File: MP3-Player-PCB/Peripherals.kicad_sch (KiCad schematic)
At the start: 27 parts, among them J301 Micro_SD_Card_Det1, Q301 AO3401A, Q302 2N7002H, SW301 1-1825910-4, SW302 1-1825910-4, SW303 1-1825910-4, SW304 1-1825910-4, U301 TPD4E1U06

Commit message: Much better initial layout
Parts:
- C301, C304, C305: footprint Capacitor_SMD:C_0805_2012Metric -> Capacitor_SMD:C_0603_1608Metric
- C302, C303: footprint Capacitor_SMD:C_0603_1608Metric -> Capacitor_SMD:C_0402_1005Metric
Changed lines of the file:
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@@
 			)
 		)
-		(property "Footprint" "Capacitor_SMD:C_0603_1608Metric"
+		(property "Footprint" "Capacitor_SMD:C_0402_1005Metric"
 			(at 42.2148 58.42 0)
 			(effects
@@
 			)
 		)
-		(property "Footprint" "Capacitor_SMD:C_0603_1608Metric"
+		(property "Footprint" "Capacitor_SMD:C_0402_1005Metric"
 			(at 71.4248 83.82 0)
 			(effects
@@
 			)
 		)
-		(property "Footprint" "Capacitor_SMD:C_0805_2012Metric"
+		(property "Footprint" "Capacitor_SMD:C_0603_1608Metric"
 			(at 29.5148 58.42 0)
 			(effects
@@
 			)
 		)
-		(property "Footprint" "Capacitor_SMD:C_0805_2012Metric"
+		(property "Footprint" "Capacitor_SMD:C_0603_1608Metric"
 			(at 99.3648 137.16 0)
 			(effects
@@
 			)
 		)
-		(property "Footprint" "Capacitor_SMD:C_0805_2012Metric"
+		(property "Footprint" "Capacitor_SMD:C_0603_1608Metric"
 			(at 136.1948 138.43 0)
 			(effects

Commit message: Cleaned up layout yet again for proper routing. Started preliminary routing
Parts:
- R305, R306, R307: footprint Resistor_SMD:R_0603_1608Metric -> Resistor_SMD:R_0402_1005Metric
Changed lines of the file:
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@@
 			)
 		)
-		(property "Footprint" "Resistor_SMD:R_0603_1608Metric"
+		(property "Footprint" "Resistor_SMD:R_0402_1005Metric"
 			(at 91.44 47.498 90)
 			(effects
@@
 			)
 		)
-		(property "Footprint" "Resistor_SMD:R_0603_1608Metric"
+		(property "Footprint" "Resistor_SMD:R_0402_1005Metric"
 			(at 91.44 57.658 90)
 			(effects
@@
 			)
 		)
-		(property "Footprint" "Resistor_SMD:R_0603_1608Metric"
+		(property "Footprint" "Resistor_SMD:R_0402_1005Metric"
 			(at 91.44 52.578 90)
 			(effects

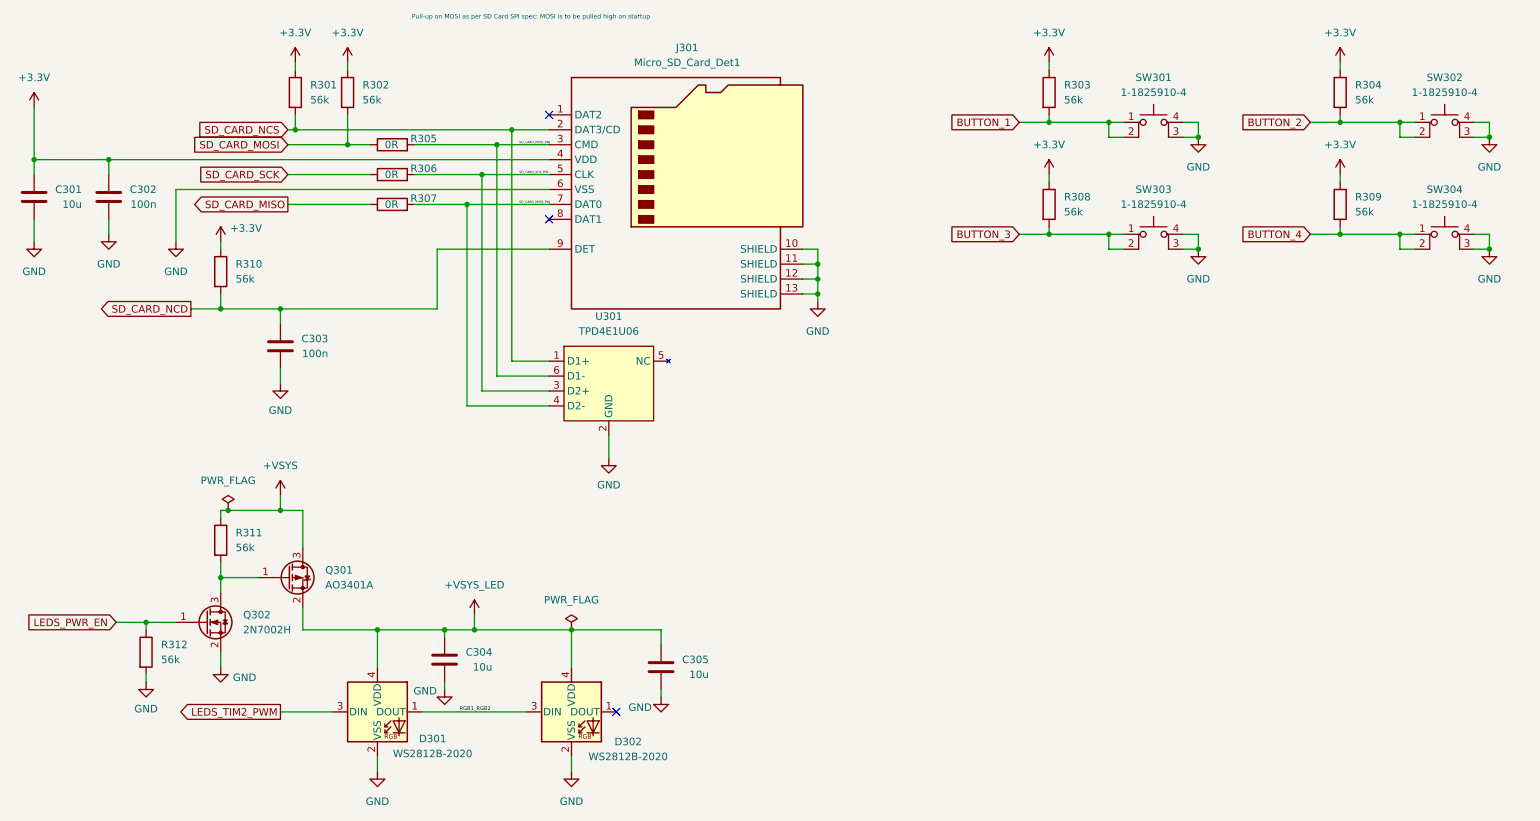
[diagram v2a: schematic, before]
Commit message: Routing more mcu signals
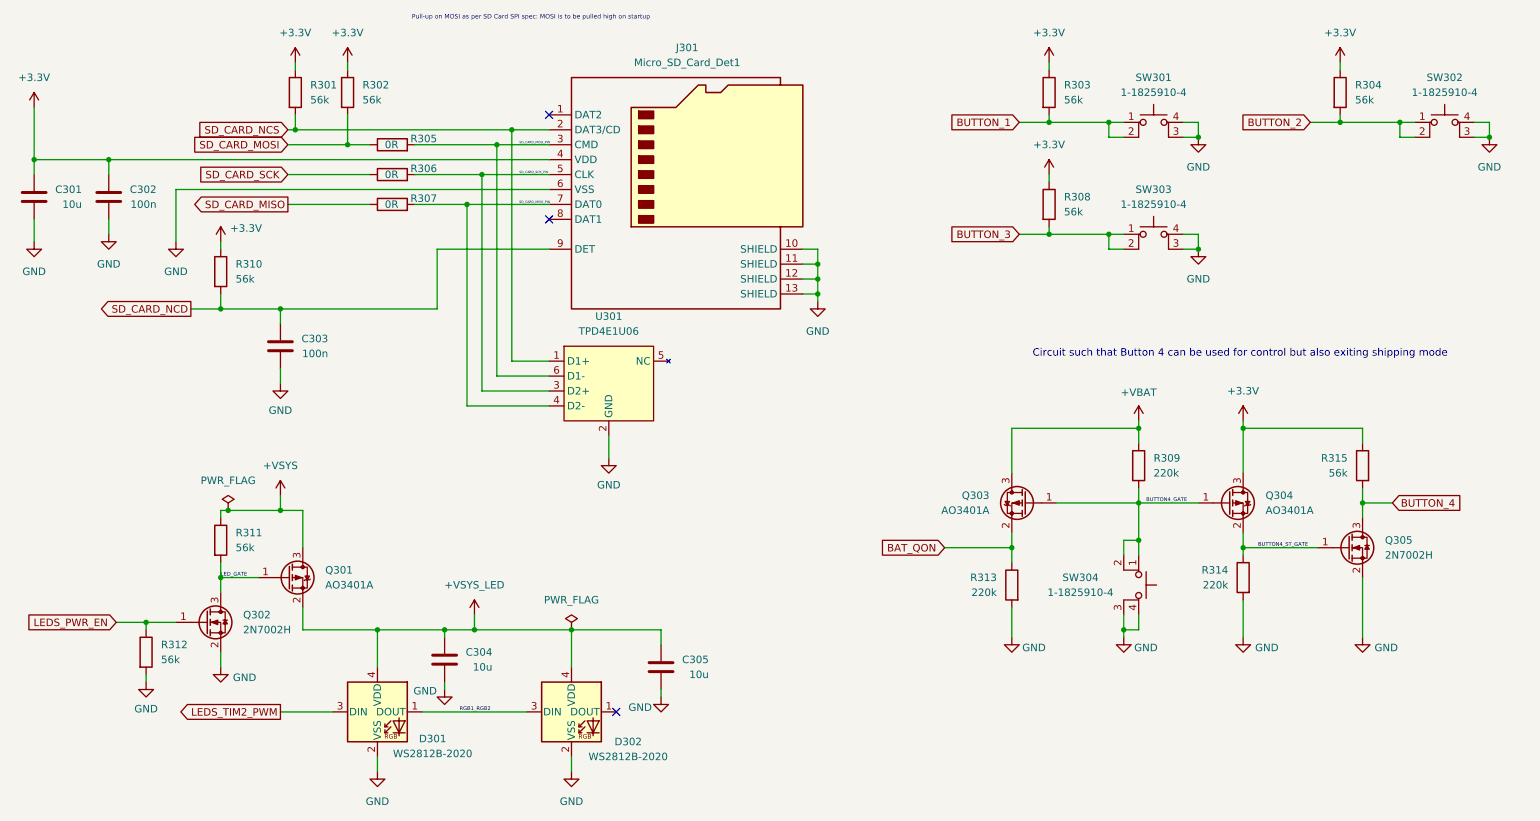
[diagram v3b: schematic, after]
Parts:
- added Q303, Q304: AO3401A, Package_TO_SOT_SMD:SOT-23, symbol Transistor_FET:AO3401A
- added Q305: 2N7002H, Package_TO_SOT_SMD:SOT-23, symbol Transistor_FET:2N7002H
- added R313, R314: 220k, Resistor_SMD:R_0402_1005Metric, symbol Device:R
- added R315: 56k, Resistor_SMD:R_0402_1005Metric, symbol Device:R
- R309: value 56k -> 220k
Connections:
- net +3.3V: now also Q304.3 (D), R315.1; no longer R309.1
- net BUTTON_4: now also Q305.3 (D), R315.2; no longer R309.2, SW304.1, SW304.2
- net GND: now also Q305.2 (S), R313.2, R314.2
- net LED_GATE: now reaches Q301.1 (G), Q302.3 (D), R311.2
- new net +VBAT: Q303.3 (D), R309.1
- new net BAT_QON: Q303.2 (S), R313.1
- new net BUTTON4_GATE: Q303.1 (G), Q304.1 (G), R309.2, SW304.1, SW304.2
- new net BUTTON4_ST_GATE: Q304.2 (S), Q305.1 (G), R314.1
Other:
- note added: "Circuit such that Button 4 can be used for control but also exiting shipping mode"
- moved on the sheet: R309, SW304

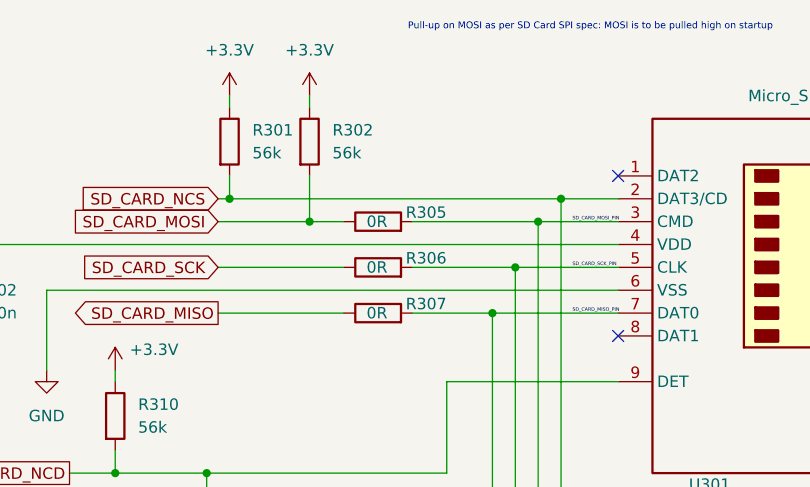
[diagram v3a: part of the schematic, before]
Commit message: Routed VBAT power trace in 3rd layer
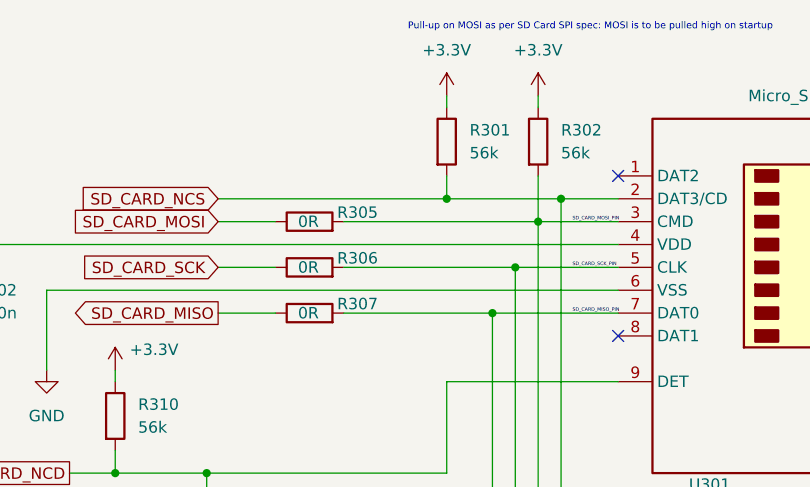
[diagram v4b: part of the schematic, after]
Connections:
- net SD_CARD_MOSI: no longer R302.2
- net SD_CARD_MOSI_PIN: now also R302.2
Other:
- moved on the sheet: R301, R302, R305, R306, R307

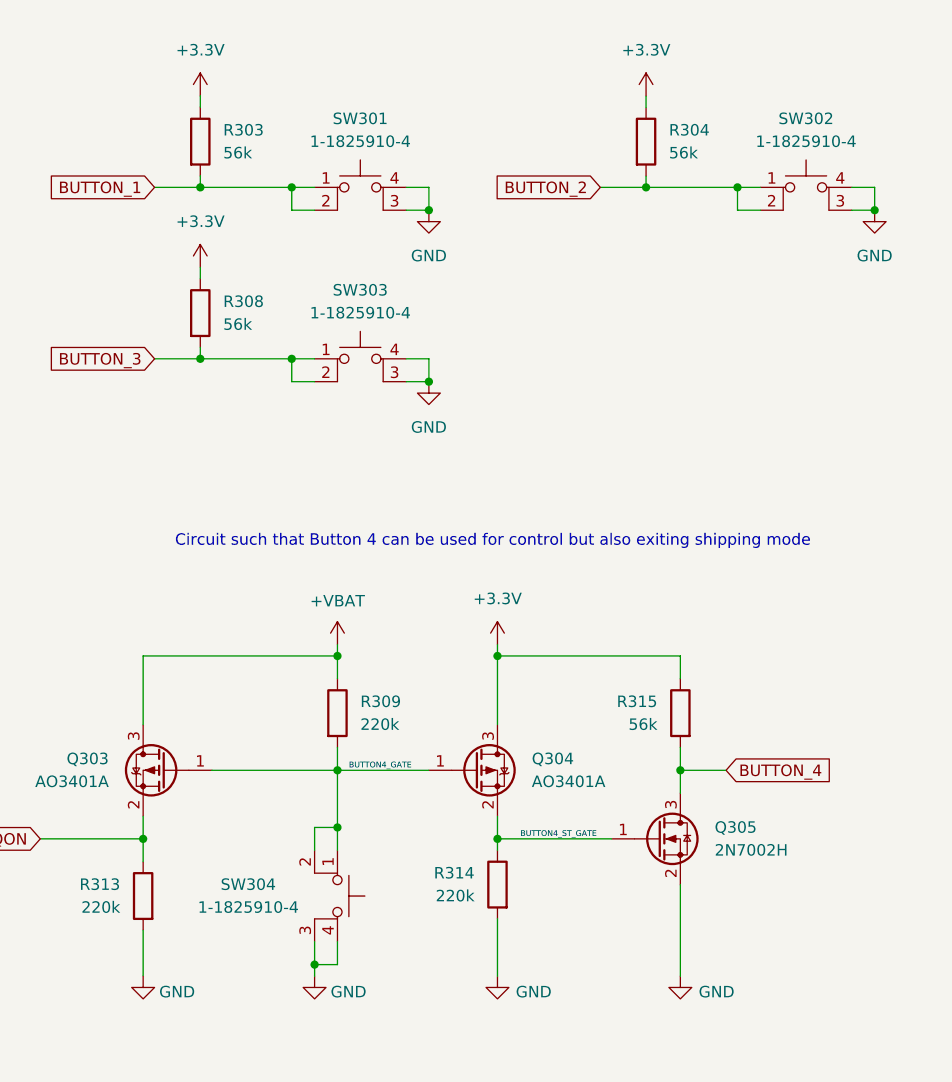
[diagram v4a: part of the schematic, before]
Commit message: Replaced THT buttons with SMT
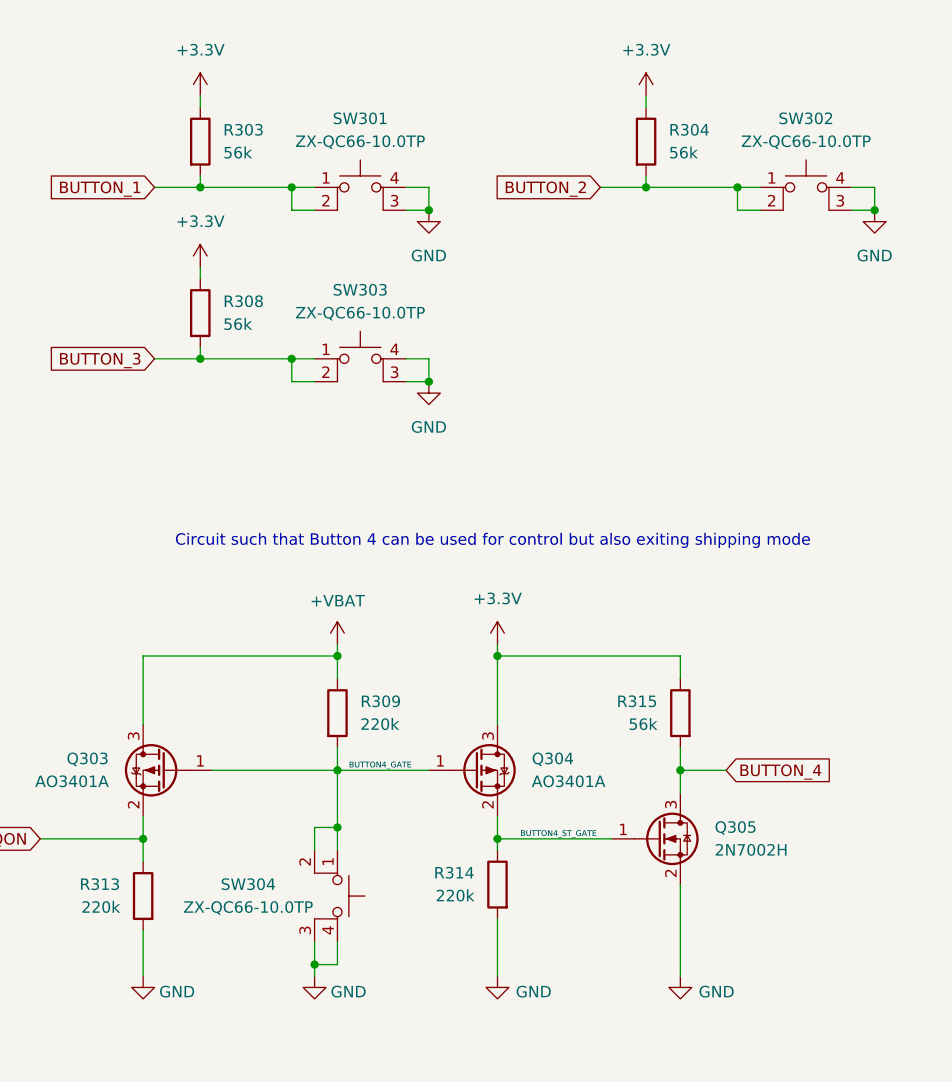
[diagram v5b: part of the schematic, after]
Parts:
- SW301, SW302, SW303, SW304: value 1-1825910-4 -> ZX-QC66-10.0TP; footprint MP3-Player_Footprint_Libraries:1-1825910-4 -> MP3-Player_Footprint_Libraries:ZX-QC66
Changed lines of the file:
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@@
 			)
 		)
-		(property "Value" "1-1825910-4"
+		(property "Value" "ZX-QC66-10.0TP"
 			(at 270.51 36.83 0)
 			(effects
@@
 			)
 		)
-		(property "Footprint" "MP3-Player_Footprint_Libraries:1-1825910-4"
+		(property "Footprint" "MP3-Player_Footprint_Libraries:ZX-QC66"
 			(at 270.51 36.83 0)
 			(effects
@@
 			)
 		)
-		(property "Value" "1-1825910-4"
+		(property "Value" "ZX-QC66-10.0TP"
 			(at 220.98 55.88 0)
 			(effects
@@
 			)
 		)
-		(property "Footprint" "MP3-Player_Footprint_Libraries:1-1825910-4"
+		(property "Footprint" "MP3-Player_Footprint_Libraries:ZX-QC66"
 			(at 220.98 55.88 0)
 			(effects
@@
 			)
 		)
-		(property "Value" "1-1825910-4"
+		(property "Value" "ZX-QC66-10.0TP"
 			(at 208.534 121.92 90)
 			(effects
@@
 			)
 		)
-		(property "Footprint" "MP3-Player_Footprint_Libraries:1-1825910-4"
+		(property "Footprint" "MP3-Player_Footprint_Libraries:ZX-QC66"
 			(at 223.52 120.65 0)
 			(effects
@@
 			)
 		)
-		(property "Value" "1-1825910-4"
+		(property "Value" "ZX-QC66-10.0TP"
 			(at 220.98 36.83 0)
 			(effects
@@
 			)
 		)
-		(property "Footprint" "MP3-Player_Footprint_Libraries:1-1825910-4"
+		(property "Footprint" "MP3-Player_Footprint_Libraries:ZX-QC66"
 			(at 220.98 36.83 0)
 			(effects

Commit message: Assigning JLCPCB part #'s
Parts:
- C301, C304, C305: JLCPCB Part # (none) -> C19702
- C302, C303: JLCPCB Part # (none) -> C1525
- D301, D302: JLCPCB Part # (none) -> C965555
- J301: JLCPCB Part # (none) -> C113206
- Q301, Q303, Q304: JLCPCB Part # (none) -> C15127
- Q302, Q305: JLCPCB Part # (none) -> C3290631
- R301, R302, R303, R304, R308, R310, R311, R312, R315: JLCPCB Part # (none) -> C25796
- R305, R306, R307: JLCPCB Part # (none) -> C17168
- R309, R313, R314: JLCPCB Part # (none) -> C25546
- SW301, SW302, SW303, SW304: JLCPCB Part # (none) -> C7470162
- U301: JLCPCB Part # (none) -> C124691
